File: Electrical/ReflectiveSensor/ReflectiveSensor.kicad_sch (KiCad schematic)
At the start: 5 parts, among them J1 Refl_Mount, K1 QRE1113GR

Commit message: Finalize Reflective Opto Sensor
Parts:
- added C1: 0.1 uF, Capacitor_SMD:C_0805_2012Metric_Pad1.18x1.45mm_HandSolder, symbol Device:C
- J1: now left out of the parts list
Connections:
- net at J1.1 (Pin_1), R1.2, R2.2: now also C1.1
- net at J1.2 (Pin_2), K1.2, K1.4: now also C1.2
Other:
- title: Test sheet -> Reflective Opto (Cliff) Sensor
- moved on the sheet: H1, J1, K1, R1, R2

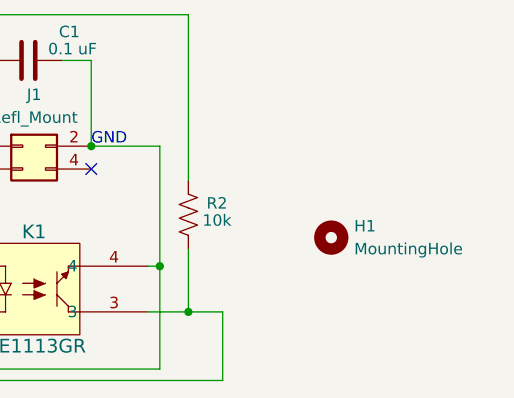
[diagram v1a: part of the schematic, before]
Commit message: Resize the reflective sensor
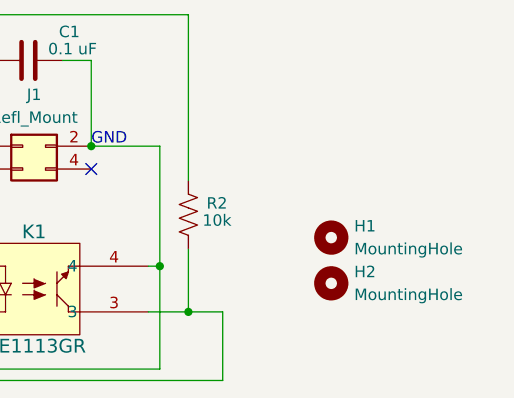
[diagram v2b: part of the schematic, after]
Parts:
- added H2: MountingHole, MountingHole:MountingHole_2.2mm_M2, symbol Mechanical:MountingHole
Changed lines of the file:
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@@
+    )
+  )
+  (symbol (lib_id "Mechanical:MountingHole") (at 267.335 160.655 0) (unit 1)
+    (in_bom no) (on_board yes) (dnp no) (fields_autoplaced)
+    (property "Reference" "H2" (at 269.875 159.385 0)
+      (effects (font (size 1.27 1.27)) (justify left))
+    )
+    (property "Value" "MountingHole" (at 269.875 161.925 0)
+      (effects (font (size 1.27 1.27)) (justify left))
+    )
+    (property "Footprint" "MountingHole:MountingHole_2.2mm_M2" (at 267.335 160.655 0)
+      (effects (font (size 1.27 1.27)) hide)
+    )
+    (property "Datasheet" "~" (at 267.335 160.655 0)
+      (effects (font (size 1.27 1.27)) hide)
+    )
+    (property "Description" "" (at 267.335 160.655 0)
+      (effects (font (size 1.27 1.27)) hide)
+    )
+    (property "Mfr" "" (at 267.335 160.655 0)
+      (effects (font (size 1.27 1.27)) hide)
+    )
+    (property "Mfr P/N" "" (at 267.335 160.655 0)
+      (effects (font (size 1.27 1.27)) hide)
+    )
+    (property "Supplier 1" "" (at 267.335 160.655 0)
+      (effects (font (size 1.27 1.27)) hide)
+    )
+    (property "Supplier 1 P/N" "" (at 267.335 160.655 0)
+      (effects (font (size 1.27 1.27)) hide)
+    )
+    (property "Supplier 2" "" (at 267.335 160.655 0)
+      (effects (font (size 1.27 1.27)) hide)
+    )
+    (property "Supplier 2 P/N" "" (at 267.335 160.655 0)
+      (effects (font (size 1.27 1.27)) hide)
+    )
+    (instances
+      (project "ReflectiveSensor"
+        (path "/1c59de6a-87fe-4223-8898-4b0383164a31"
+          (reference "H2") (unit 1)
+        )
+      )
+      (project "MainBoard"
+        (path "/bd24c4db-4e36-4117-bd4f-5228ef241da9/c568ceec-b7ac-45ca-9b64-1ad9e4a2513b"
+          (reference "H5") (unit 1)
+        )
+      )
+      (project "OtherSensors"
+        (path "/c8948736-9ac9-494c-8aa2-474939e1a0e8"
+          (reference "H5") (unit 1)
+        )
+      )
     )
   )
